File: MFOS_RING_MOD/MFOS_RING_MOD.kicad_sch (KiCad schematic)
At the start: 111 parts, among them J1 Barrel_Jack, J10 Conn_01x01, J11 Conn_01x01, J12 Conn_01x01, J13 Conn_01x01, J14 Conn_01x01, J15 Conn_01x01, J16 Conn_01x01, J17 Conn_01x01, J18 Conn_01x01, J19 Conn_01x01, J2 Barrel_Jack, J20 Conn_01x01, J21 Conn_01x01, J22 Conn_01x01, J23 Conn_01x01, J24 Conn_01x01, J25 Conn_01x01, J26 Conn_01x01, J27 Conn_01x01, J28 Conn_01x01, J3 Barrel_Jack, J4 Barrel_Jack, J5 Barrel_Jack, J6 Barrel_Jack, J7 Conn_01x01, J8 Conn_01x01, J9 Conn_01x01, Q1 2N3906, Q2 2N3906, Q3 2N3906, U1 TL084, U2 LM13700, U3 TL084, U4 TL084, U5 AD633

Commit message: Reviewed BOM
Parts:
- removed R16: 50K, symbol Device:R_Potentiometer
- added R16: 50K, symbol Device:R_Potentiometer_Trim
- J10, J11, J12, J13, J14, J15, J16, J17, J18, J19, J20, J21, J22, J23, J24, J25, J26, J27, J28, J7, J8, J9: now left out of the parts list
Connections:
- net +12V: now also R16.3
- net -12V: now also R16.1
- net at R10.1: now also R16.2

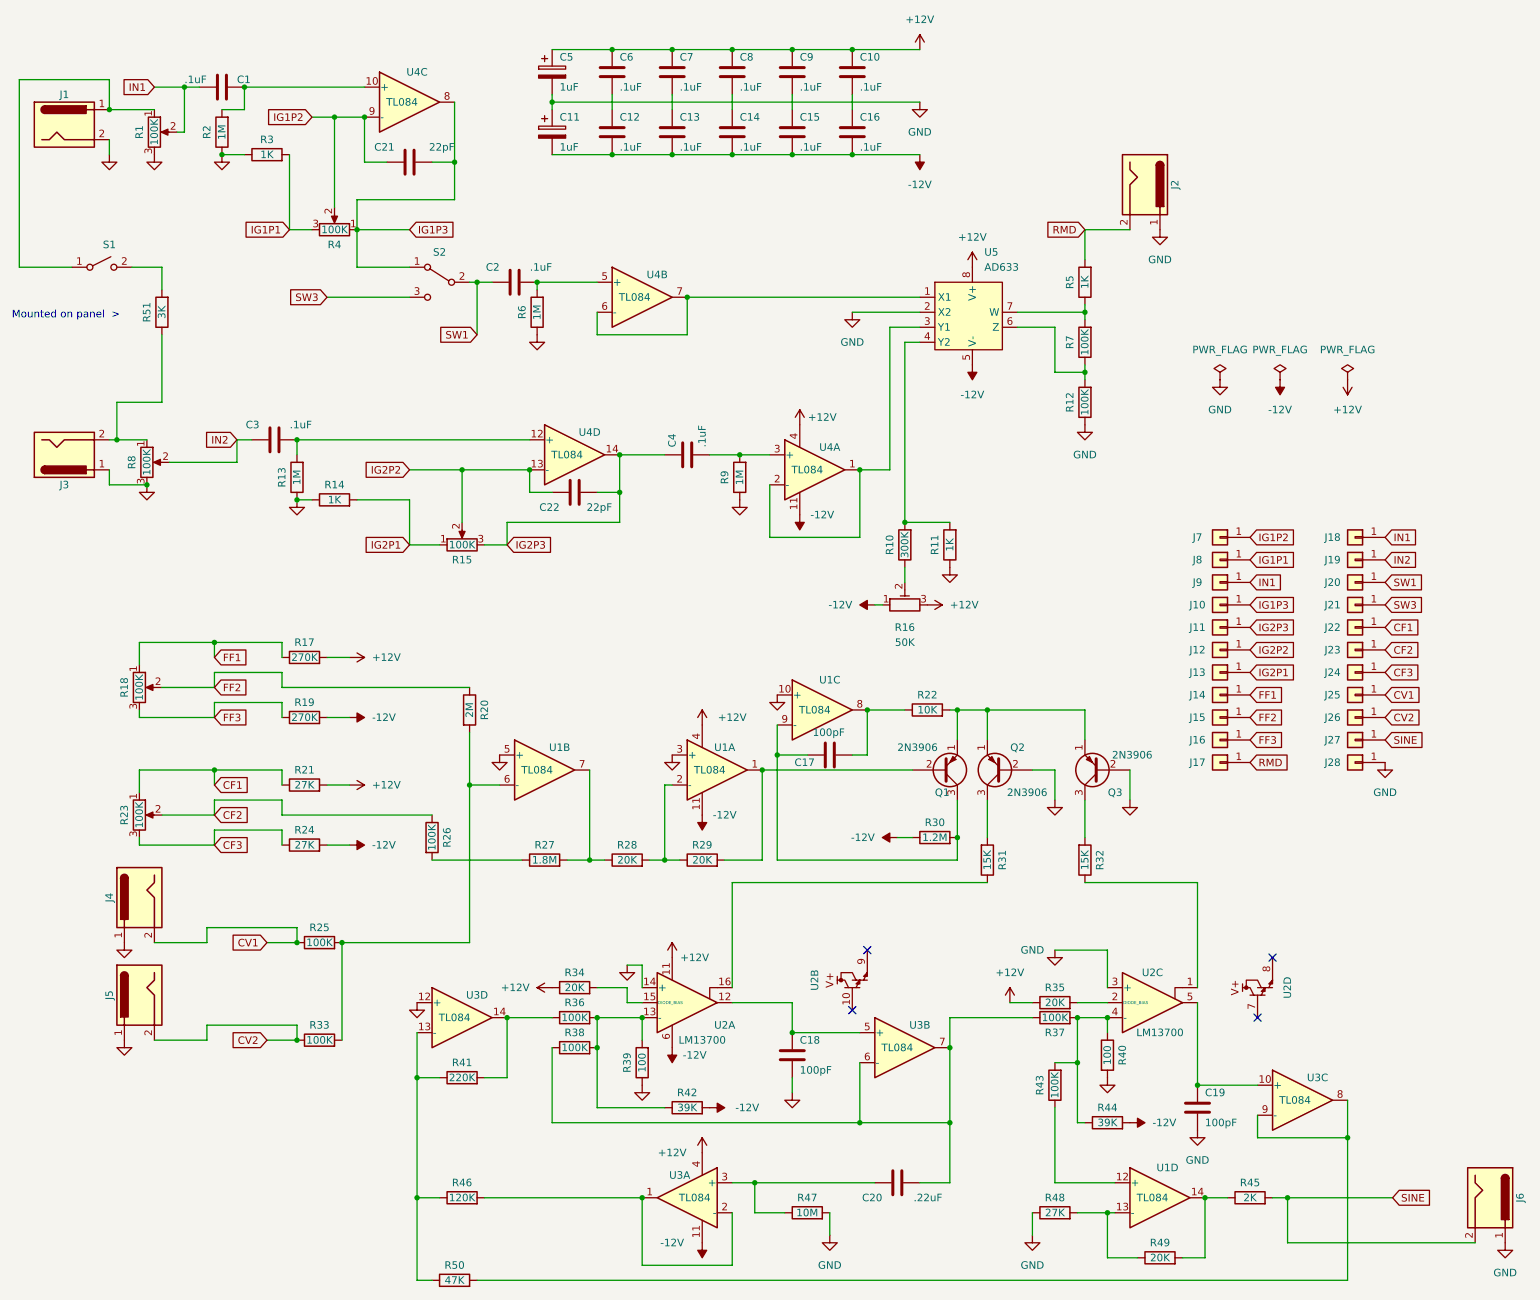
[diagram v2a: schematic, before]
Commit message: Designs adapted for BOM
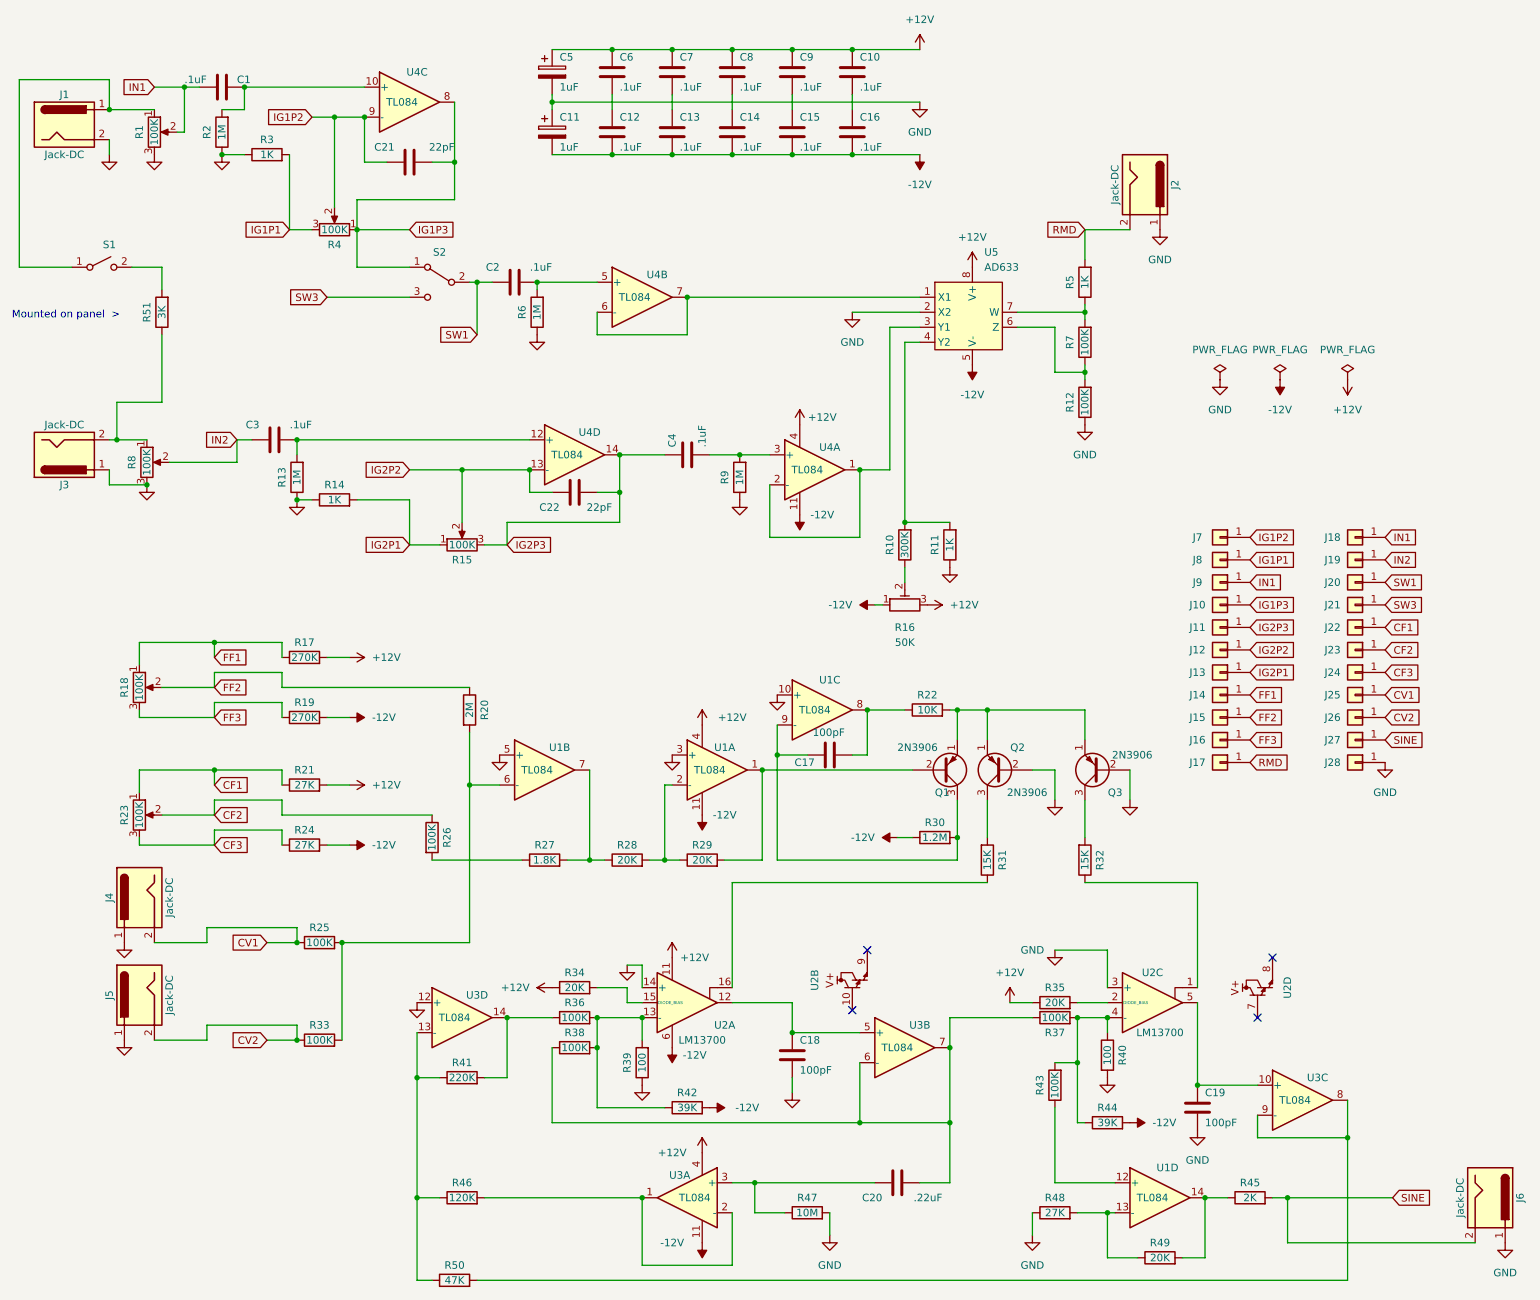
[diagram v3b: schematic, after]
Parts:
- J1, J2, J3, J4, J5, J6: value Barrel_Jack -> Jack-DC; symbol Connector:Barrel_Jack -> Connector:Jack-DC
- R16: symbol Device:R_Potentiometer_Trim -> dhk:R_Potentiometer_Trim
- R27: value 1.8M -> 1.8K
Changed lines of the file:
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@@
     (pin "1")
   )
-  (symbol (lib_id "Connector:Barrel_Jack") (at 273.05 218.44 270) (unit 1)
-    (in_bom yes) (on_board no)
+  (symbol (lib_id "Connector:Jack-DC") (at 273.05 218.44 270) (unit 1)
+    (in_bom yes) (on_board yes)
     (property "Reference" "J6" (id 0) (at 278.13 218.44 0))
-    (property "Value" "Barrel_Jack" (id 1) (at 279.4 218.44 0)
-      (effects (font (size 1.27 1.27)) hide)
-    )
+    (property "Value" "Jack-DC" (id 1) (at 267.97 218.44 0))
     (property "Footprint" "" (id 2) (at 272.034 219.71 0)
       (effects (font (size 1.27 1.27)) hide)
@@
     (pin "2")
   )
-  (symbol (lib_id "Connector:Barrel_Jack") (at 44.45 167.64 90) (mirror x) (unit 1)
-    (in_bom yes) (on_board no)
+  (symbol (lib_id "Connector:Jack-DC") (at 44.45 167.64 90) (mirror x) (unit 1)
+    (in_bom yes) (on_board yes)
     (property "Reference" "J4" (id 0) (at 39.37 167.64 0))
-    (property "Value" "Barrel_Jack" (id 1) (at 38.1 167.64 0)
-      (effects (font (size 1.27 1.27)) hide)
-    )
+    (property "Value" "Jack-DC" (id 1) (at 49.53 167.64 0))
     (property "Footprint" "" (id 2) (at 45.466 168.91 0)
       (effects (font (size 1.27 1.27)) hide)
@@
     (pin "1")
   )
-  (symbol (lib_id "Connector:Barrel_Jack") (at 44.45 184.15 90) (mirror x) (unit 1)
-    (in_bom yes) (on_board no)
+  (symbol (lib_id "Connector:Jack-DC") (at 44.45 184.15 90) (mirror x) (unit 1)
+    (in_bom yes) (on_board yes)
     (property "Reference" "J5" (id 0) (at 39.37 184.15 0))
-    (property "Value" "Barrel_Jack" (id 1) (at 38.1 184.15 0)
-      (effects (font (size 1.27 1.27)) hide)
-    )
+    (property "Value" "Jack-DC" (id 1) (at 49.53 184.15 0))
     (property "Footprint" "" (id 2) (at 45.466 185.42 0)
       (effects (font (size 1.27 1.27)) hide)
@@
     (pin "1")
   )
-  (symbol (lib_id "Device:R_Potentiometer_Trim") (at 173.99 118.11 90) (unit 1)
+  (symbol (lib_id "dhk:R_Potentiometer_Trim") (at 173.99 118.11 90) (unit 1)
     (in_bom yes) (on_board yes) (fields_autoplaced)
     (property "Reference" "R16" (id 0) (at 173.99 121.92 90))
@@
     (pin "1")
   )
-  (symbol (lib_id "Connector:Barrel_Jack") (at 31.75 36.83 0) (unit 1)
-    (in_bom yes) (on_board no)
+  (symbol (lib_id "Connector:Jack-DC") (at 31.75 36.83 0) (unit 1)
+    (in_bom yes) (on_board yes)
     (property "Reference" "J1" (id 0) (at 31.75 31.75 0))
-    (property "Value" "Barrel_Jack" (id 1) (at 31.75 30.48 0)
-      (effects (font (size 1.27 1.27)) hide)
-    )
+    (property "Value" "Jack-DC" (id 1) (at 31.75 41.91 0))
     (property "Footprint" "" (id 2) (at 33.02 37.846 0)
       (effects (font (size 1.27 1.27)) hide)
@@
     (pin "2")
   )
-  (symbol (lib_id "Connector:Barrel_Jack") (at 214.63 46.99 270) (unit 1)
-    (in_bom yes) (on_board no)
+  (symbol (lib_id "Connector:Jack-DC") (at 214.63 46.99 270) (unit 1)
+    (in_bom yes) (on_board yes)
     (property "Reference" "J2" (id 0) (at 219.71 46.99 0))
-    (property "Value" "Barrel_Jack" (id 1) (at 220.98 46.99 0)
-      (effects (font (size 1.27 1.27)) hide)
-    )
+    (property "Value" "Jack-DC" (id 1) (at 209.55 46.99 0))
     (property "Footprint" "" (id 2) (at 213.614 48.26 0)
       (effects (font (size 1.27 1.27)) hide)
@@
     (pin "2")
   )
-  (symbol (lib_id "Connector:Barrel_Jack") (at 31.75 92.71 0) (mirror x) (unit 1)
-    (in_bom yes) (on_board no)
+  (symbol (lib_id "Connector:Jack-DC") (at 31.75 92.71 0) (mirror x) (unit 1)
+    (in_bom yes) (on_board yes)
     (property "Reference" "J3" (id 0) (at 31.75 97.79 0))
-    (property "Value" "Barrel_Jack" (id 1) (at 31.75 99.06 0)
-      (effects (font (size 1.27 1.27)) hide)
-    )
+    (property "Value" "Jack-DC" (id 1) (at 31.75 87.63 0))
     (property "Footprint" "" (id 2) (at 33.02 91.694 0)
       (effects (font (size 1.27 1.27)) hide)
@@
     (in_bom yes) (on_board yes)
     (property "Reference" "R27" (id 0) (at 113.03 158.75 90))
-    (property "Value" "1.8M" (id 1) (at 113.03 161.29 90))
+    (property "Value" "1.8K" (id 1) (at 113.03 161.29 90))
     (property "Footprint" "" (id 2) (at 113.03 163.068 90)
       (effects (font (size 1.27 1.27)) hide)
@@
     )
     (path "/8ddaf12a-7bd8-481a-a443-e2cd3e8ff093"
-      (reference "J1") (unit 1) (value "Barrel_Jack") (footprint "")
+      (reference "J1") (unit 1) (value "Jack-DC") (footprint "")
     )
     (path "/b1c34899-6b12-4166-9455-593f486d378b"
-      (reference "J2") (unit 1) (value "Barrel_Jack") (footprint "")
+      (reference "J2") (unit 1) (value "Jack-DC") (footprint "")
     )
     (path "/f0351bd2-8ecf-43e3-88b0-8b098da54de0"
-      (reference "J3") (unit 1) (value "Barrel_Jack") (footprint "")
+      (reference "J3") (unit 1) (value "Jack-DC") (footprint "")
     )
     (path "/403fd629-e2d4-45b1-9460-61f1973a54b5"
-      (reference "J4") (unit 1) (value "Barrel_Jack") (footprint "")
+      (reference "J4") (unit 1) (value "Jack-DC") (footprint "")
     )
     (path "/4e6db472-a629-4005-bcb4-8ec44101d7b9"
-      (reference "J5") (unit 1) (value "Barrel_Jack") (footprint "")
+      (reference "J5") (unit 1) (value "Jack-DC") (footprint "")
     )
     (path "/3a8251bb-2ba0-40ea-888e-23daf4abf5e0"
-      (reference "J6") (unit 1) (value "Barrel_Jack") (footprint "")
+      (reference "J6") (unit 1) (value "Jack-DC") (footprint "")
     )
     (path "/eb8f52c6-9883-4ba9-819c-52db1217c771"
@@
     )
     (path "/f6cfad62-afb8-4880-9e23-872b0577db06"
-      (reference "R27") (unit 1) (value "1.8M") (footprint "")
+      (reference "R27") (unit 1) (value "1.8K") (footprint "")
     )
     (path "/b5e415ca-2e05-4db7-b81e-7ab91eda14e4"
